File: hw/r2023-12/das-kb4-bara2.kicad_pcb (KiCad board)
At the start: 4 copper layers, 94 x 52 mm, 68 parts, among them J1 USB_A, J2 USB_A, J3 Conn_01x26_Socket, J4 USB_C_Receptacle_USB2.0, J5 Conn_ARM_JTAG_SWD_10, J6 Conn_01x06_Socket, J7 Conn_02x04_Odd_Even, SW1 PWR, SW2 MUTE, SW3 PREV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

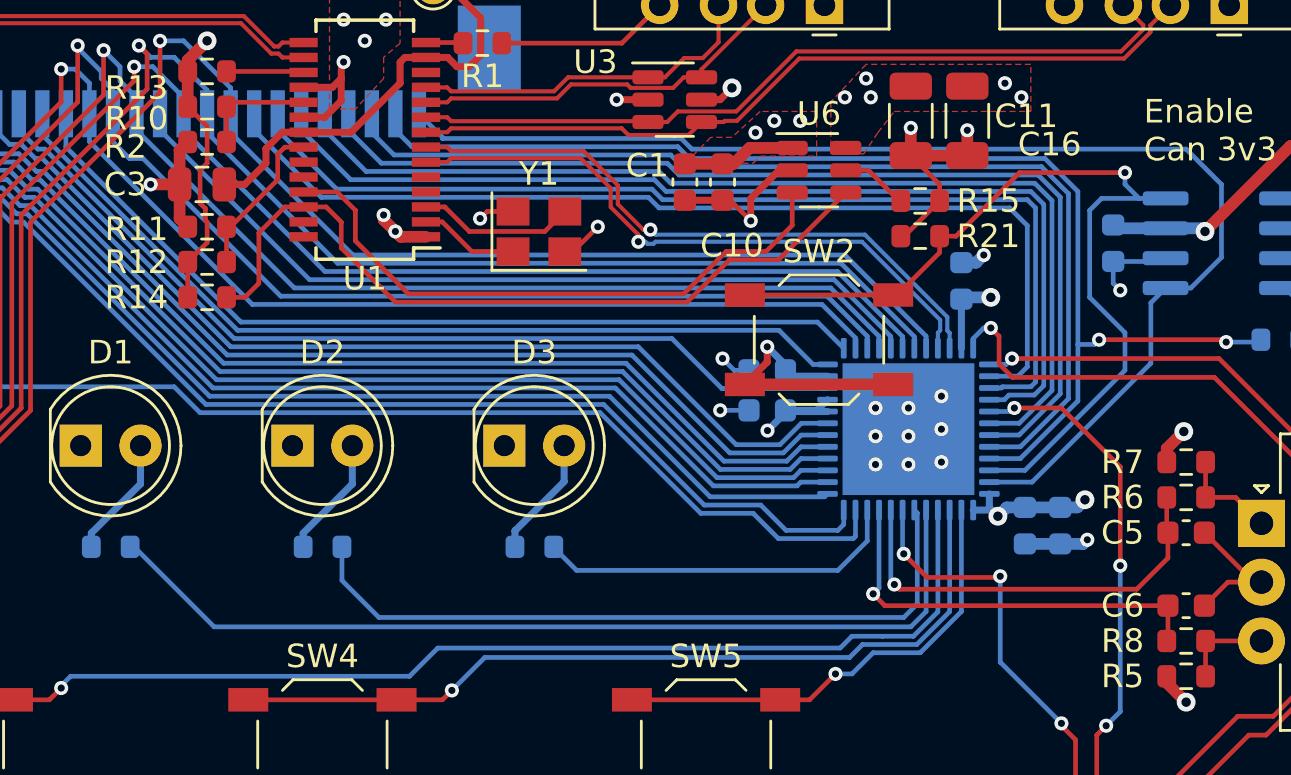
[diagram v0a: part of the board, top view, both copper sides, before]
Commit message: r2023-12: one last silk update
We're just going to pay to get a rev done.  merry christmas me or
something.  no more faffing about, just get a revision back and stop
wasting time.
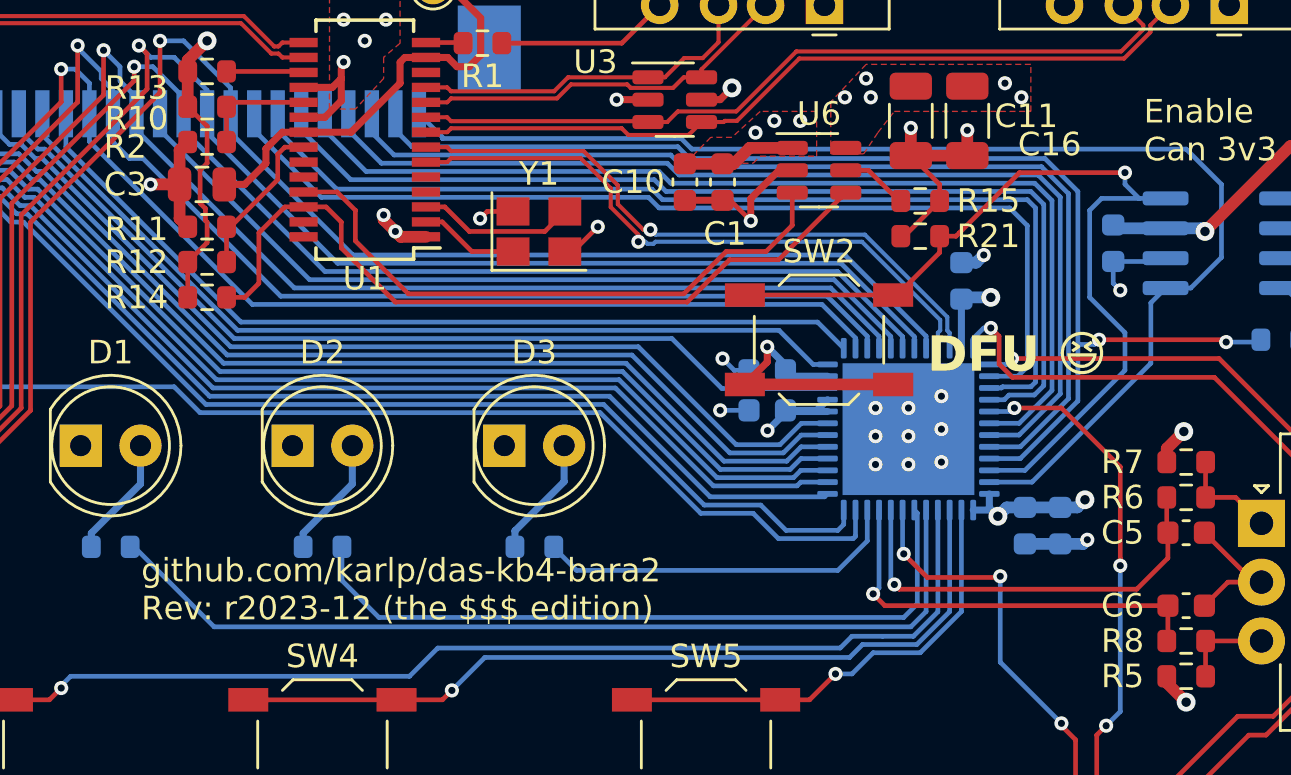
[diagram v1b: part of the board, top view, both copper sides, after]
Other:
- board text added: "DFU 😆"
- board text added: "github.com/karlp/das-kb4-bara2 Rev: r2023-12 (the $$$ edition)"
- board text removed: "github.com/karlp/das-kb4-bara2 Rev: r2023-12"

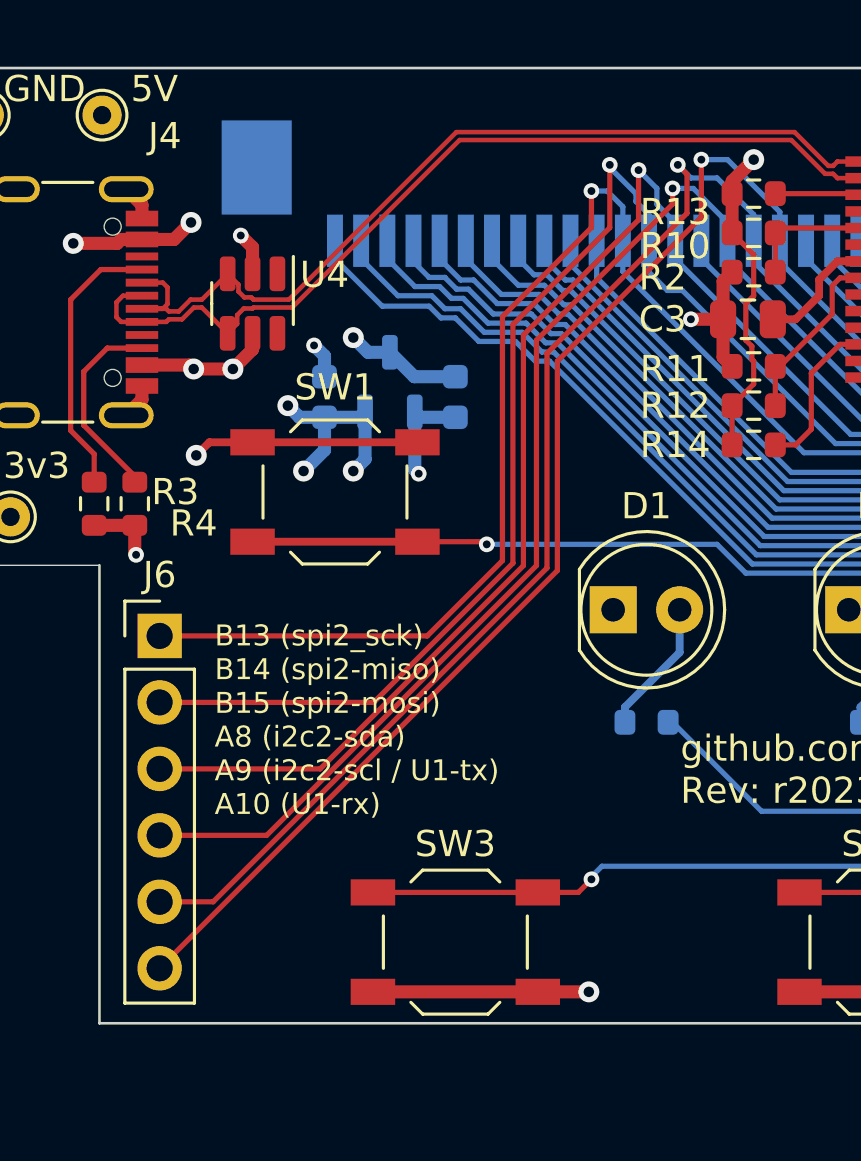
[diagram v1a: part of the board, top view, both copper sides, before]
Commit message: r2023-12: add more gnd pins
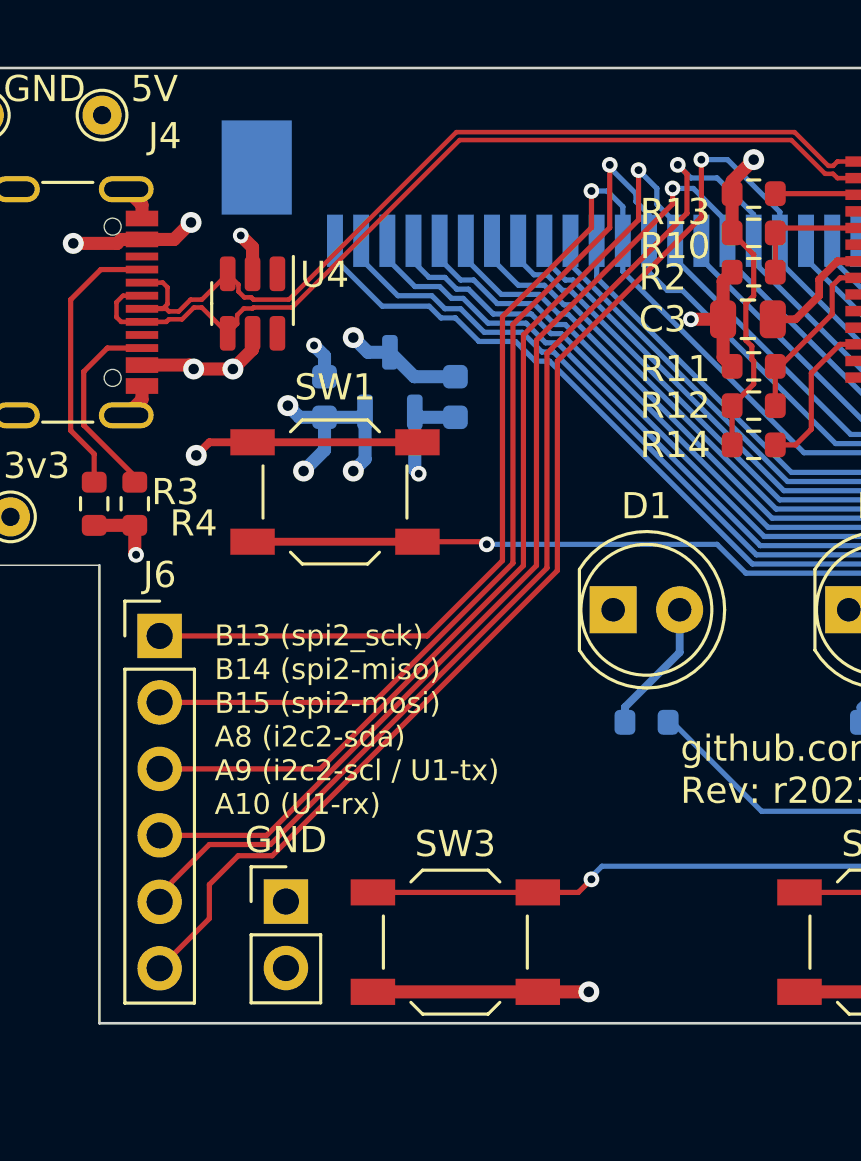
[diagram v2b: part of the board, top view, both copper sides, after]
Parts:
- added JP3: GND, Connector_PinHeader_2.54mm:PinHeader_1x02_P2.54mm_Vertical, F.Cu at (110.5, 120.7)
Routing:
- net /keys_mcu/CM25: track 78.9 -> 79.6 mm
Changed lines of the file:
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@@
     (property "Sheetfile" "das-kb4-bara2.kicad_sch")
     (property "Sheetname" "")
+    (property "exclude_from_bom" "")
     (property "ki_description" "test point")
     (property "ki_keywords" "test point tp")
     (property "lcsc2#" "")
-    (attr exclude_from_pos_files)
+    (attr exclude_from_pos_files exclude_from_bom)
     (fp_text reference "TP2" (at 0 -1.648) (layer "F.SilkS") hide
         (effects (font (size 1 1) (thickness 0.15)))
@@
     (property "Sheetfile" "das-kb4-bara2.kicad_sch")
     (property "Sheetname" "")
+    (property "exclude_from_bom" "")
     (property "ki_description" "test point")
     (property "ki_keywords" "test point tp")
     (property "lcsc2#" "")
-    (attr exclude_from_pos_files)
+    (attr exclude_from_pos_files exclude_from_bom)
     (fp_text reference "TP1" (at 2.3 -1) (layer "F.SilkS") hide
         (effects (font (size 1 1) (thickness 0.15)))
@@
     (property "Sheetfile" "usb.kicad_sch")
     (property "Sheetname" "usb")
+    (property "exclude_from_bom" "")
     (property "ki_description" "test point")
     (property "ki_keywords" "test point tp")
     (property "lcsc2#" "")
-    (attr exclude_from_pos_files)
+    (attr exclude_from_pos_files exclude_from_bom)
     (fp_text reference "TP4" (at 0 -1.648) (layer "F.SilkS") hide
         (effects (font (size 1 1) (thickness 0.15)))
@@
     )
   )
+  (footprint "Connector_PinHeader_2.54mm:PinHeader_1x02_P2.54mm_Vertical" (layer "F.Cu")
+    (at 110.525 120.65)
+    (descr "Through hole straight pin header, 1x02, 2.54mm pitch, single row")
+    (tags "Through hole pin header THT 1x02 2.54mm single row")
+    (property "Sheetfile" "keys_mcu.kicad_sch")
+    (property "Sheetname" "keys_mcu")
+    (property "ki_description" "Jumper, 2-pole, open")
+    (property "ki_keywords" "Jumper SPST")
+    (attr through_hole)
+    (fp_text reference "JP3" (at 0 -2.33) (layer "F.SilkS") hide
+        (effects (font (size 1 1) (thickness 0.15)))
+    )
+    (fp_text value "GND" (at 0 -2.35) (layer "F.SilkS")
+        (effects (font (size 1 1) (thickness 0.15)))
+    )
+    (fp_text user "${REFERENCE}" (at 0 1.27 90) (layer "F.Fab")
+        (effects (font (size 1 1) (thickness 0.15)))
+    )
+    (fp_line (start -1.33 -1.33) (end 0 -1.33)
+      (stroke (width 0.12) (type solid)) (layer "F.SilkS"))
+    (fp_line (start -1.33 0) (end -1.33 -1.33)
+      (stroke (width 0.12) (type solid)) (layer "F.SilkS"))
+    (fp_line (start -1.33 1.27) (end -1.33 3.87)
+      (stroke (width 0.12) (type solid)) (layer "F.SilkS"))
+    (fp_line (start -1.33 1.27) (end 1.33 1.27)
+      (stroke (width 0.12) (type solid)) (layer "F.SilkS"))
+    (fp_line (start -1.33 3.87) (end 1.33 3.87)
+      (stroke (width 0.12) (type solid)) (layer "F.SilkS"))
+    (fp_line (start 1.33 1.27) (end 1.33 3.87)
+      (stroke (width 0.12) (type solid)) (layer "F.SilkS"))
+    (fp_line (start -1.8 -1.8) (end -1.8 4.35)
+      (stroke (width 0.05) (type solid)) (layer "F.CrtYd"))
+    (fp_line (start -1.8 4.35) (end 1.8 4.35)
+      (stroke (width 0.05) (type solid)) (layer "F.CrtYd"))
+    (fp_line (start 1.8 -1.8) (end -1.8 -1.8)
+      (stroke (width 0.05) (type solid)) (layer "F.CrtYd"))
+    (fp_line (start 1.8 4.35) (end 1.8 -1.8)
+      (stroke (width 0.05) (type solid)) (layer "F.CrtYd"))
+    (fp_line (start -1.27 -0.635) (end -0.635 -1.27)
+      (stroke (width 0.1) (type solid)) (layer "F.Fab"))
+    (fp_line (start -1.27 3.81) (end -1.27 -0.635)
+      (stroke (width 0.1) (type solid)) (layer "F.Fab"))
+    (fp_line (start -0.635 -1.27) (end 1.27 -1.27)
+      (stroke (width 0.1) (type solid)) (layer "F.Fab"))
+    (fp_line (start 1.27 -1.27) (end 1.27 3.81)
+      (stroke (width 0.1) (type solid)) (layer "F.Fab"))
+    (fp_line (start 1.27 3.81) (end -1.27 3.81)
+      (stroke (width 0.1) (type solid)) (layer "F.Fab"))
+    (pad "1" thru_hole rect (at 0 0) (size 1.7 1.7) (drill 1) (layers "*.Cu" "*.Mask")
+      (net 1 "GND") (pinfunction "A") (pintype "passive"))
+    (pad "2" thru_hole oval (at 0 2.54) (size 1.7 1.7) (drill 1) (layers "*.Cu" "*.Mask")
+      (net 1 "GND") (pinfunction "B") (pintype "passive"))
+    (model "${KICAD6_3DMODEL_DIR}/Connector_PinHeader_2.54mm.3dshapes/PinHeader_1x02_P2.54mm_Vertical.wrl"
+      (offset (xyz 0 0 0))
+      (scale (xyz 1 1 1))
+      (rotate (xyz 0 0 0))
+    )
+  )
   (footprint "Capacitor_SMD:C_0603_1608Metric" (layer "F.Cu")
     (at 180 89.1 180)
@@
     (property "Sheetfile" "das-kb4-bara2.kicad_sch")
     (property "Sheetname" "")
+    (property "exclude_from_bom" "")
     (property "ki_description" "test point")
     (property "ki_keywords" "test point tp")
     (property "lcsc2#" "")
-    (attr exclude_from_pos_files)
+    (attr exclude_from_pos_files exclude_from_bom)
     (fp_text reference "TP3" (at 2.1 -1) (layer "F.SilkS") hide
         (effects (font (size 1 1) (thickness 0.15)))
@@
   (segment (start 157.95 104.865077) (end 155.184924 102.1) (width 0.2) (layer "B.Cu") (net 38))
   (segment (start 125.85 92.85) (end 125.5 92.5) (width 0.2) (layer "F.Cu") (net 39))
-  (segment (start 105.7 120.66) (end 107.745026 120.66) (width 0.2) (layer "F.Cu") (net 39))
+  (segment (start 107.6 118.47) (end 105.7 120.37) (width 0.2) (layer "F.Cu") (net 39))
+  (segment (start 120.5 107.905026) (end 109.935027 118.47) (width 0.2) (layer "F.Cu") (net 39))
   (segment (start 120.5 107.905026) (end 120.5 99.7) (width 0.2) (layer "F.Cu") (net 39))
-  (segment (start 107.745026 120.66) (end 120.5 107.905026) (width 0.2) (layer "F.Cu") (net 39))
   (segment (start 120.5 99.7) (end 125.85 94.35) (width 0.2) (layer "F.Cu") (net 39))
+  (segment (start 109.935027 118.47) (end 107.6 118.47) (width 0.2) (layer "F.Cu") (net 39))
   (segment (start 125.85 94.35) (end 125.85 92.85) (width 0.2) (layer "F.Cu") (net 39))
+  (segment (start 105.7 120.37) (end 105.7 120.66) (width 0.2) (layer "F.Cu") (net 39))
   (via (at 125.5 92.5) (size 0.6) (drill 0.3) (layers "F.Cu" "B.Cu") (net 39))
   (segment (start 126 93) (end 125.5 92.5) (width 0.2) (layer "B.Cu") (net 39))
@@
   (segment (start 155.329898 101.75) (end 133.945 101.75) (width 0.2) (layer "B.Cu") (net 39))
   (segment (start 128.4 96.205) (end 128.4 95.4) (width 0.2) (layer "B.Cu") (net 39))
-  (segment (start 120.897487 108.002513) (end 120.897487 100.002513) (width 0.2) (layer "F.Cu") (net 40))
-  (segment (start 120.897487 100.002513) (end 126.4 94.5) (width 0.2) (layer "F.Cu") (net 40))
-  (segment (start 126.4 94.5) (end 126.4 92.3) (width 0.2) (layer "F.Cu") (net 40))
-  (segment (start 105.7 123.2) (end 120.897487 108.002513) (width 0.2) (layer "F.Cu") (net 40))
+  (segment (start 120.897487 100.002513) (end 120.897487 108.002513) (width 0.2) (layer "F.Cu") (net 40))
+  (segment (start 107.6 120) (end 107.6 121.3) (width 0.2) (layer "F.Cu") (net 40))
+  (segment (start 126.4 92.3) (end 126.4 94.5) (width 0.2) (layer "F.Cu") (net 40))
+  (segment (start 108.7 118.9) (end 107.6 120) (width 0.2) (layer "F.Cu") (net 40))
+  (segment (start 107.6 121.3) (end 105.7 123.2) (width 0.2) (layer "F.Cu") (net 40))
+  (segment (start 120.897487 108.002513) (end 110 118.9) (width 0.2) (layer "F.Cu") (net 40))
+  (segment (start 110 118.9) (end 108.7 118.9) (width 0.2) (layer "F.Cu") (net 40))
+  (segment (start 126.4 94.5) (end 120.897487 100.002513) (width 0.2) (layer "F.Cu") (net 40))
   (via (at 126.4 92.3) (size 0.6) (drill 0.3) (layers "F.Cu" "B.Cu") (net 40))
   (segment (start 129.4 95.4) (end 129.4 94.3) (width 0.2) (layer "B.Cu") (net 40))
